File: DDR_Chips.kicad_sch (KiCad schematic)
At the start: 14 parts

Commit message: fix warnings
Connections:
- net DDR_BG0 renamed DDR4_BG0
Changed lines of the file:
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@@
     (effects (font (size 1.27 1.27)) (justify right))
   )
-  (hierarchical_label "DDR_BG0" (shape input) (at 30.48 96.52 180) (fields_autoplaced)
+  (hierarchical_label "DDR4_BG0" (shape input) (at 30.48 96.52 180) (fields_autoplaced)
     (effects (font (size 1.27 1.27)) (justify right))
   )

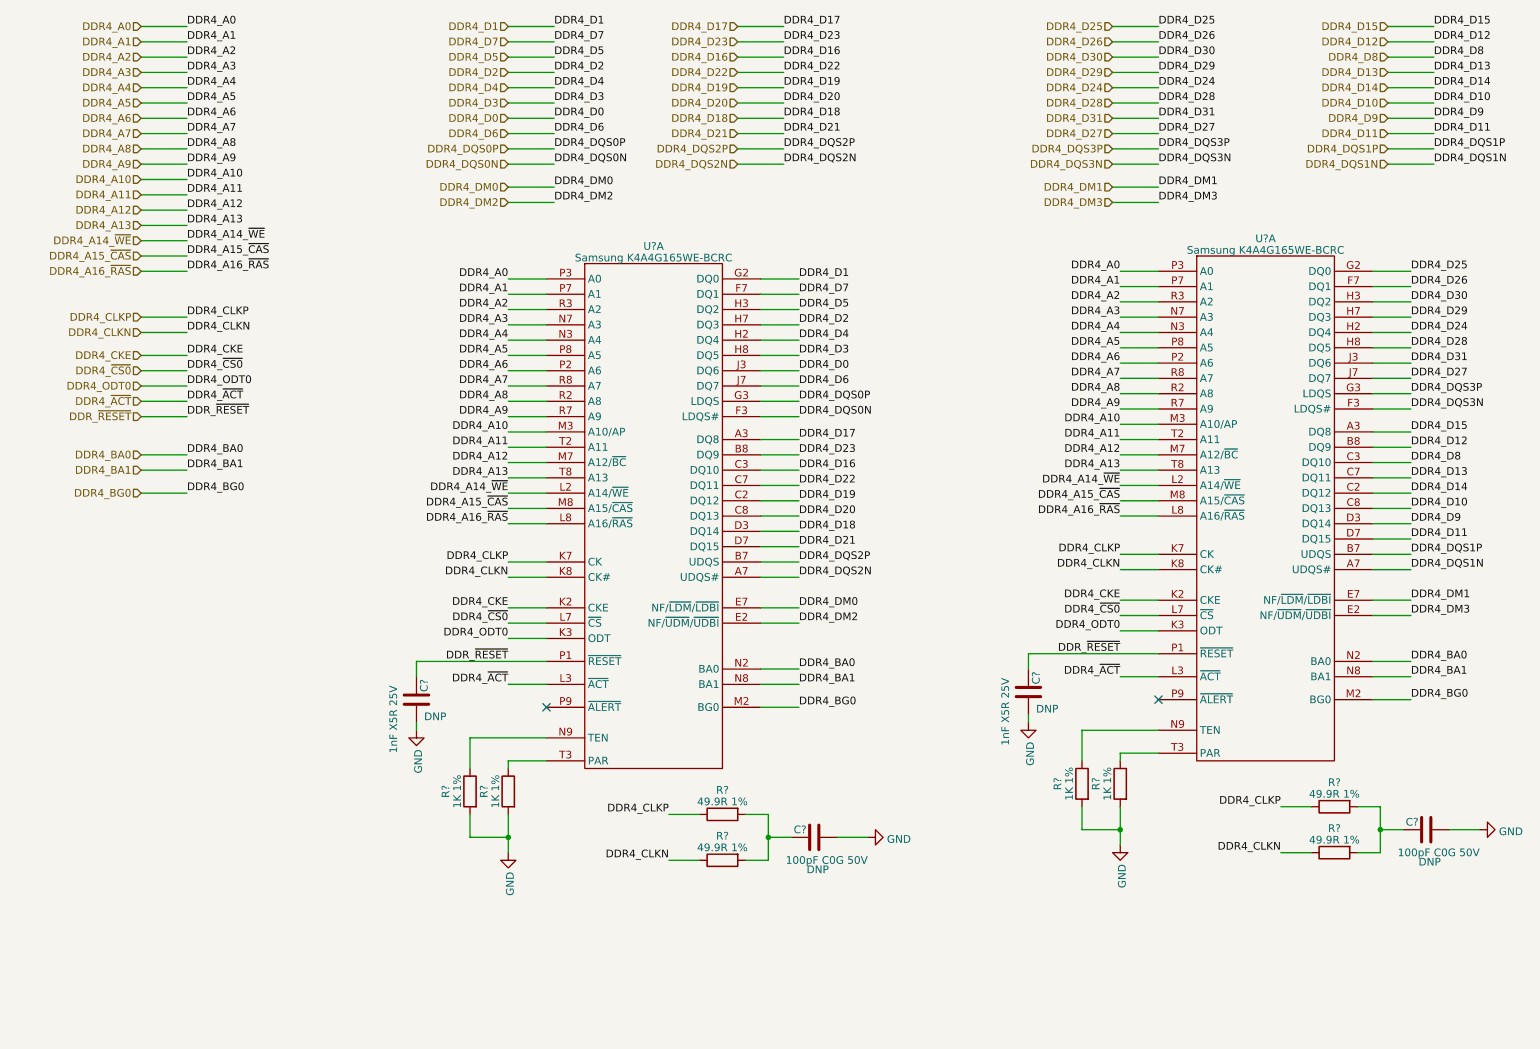
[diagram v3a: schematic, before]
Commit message: replace DDR4 chips with Hierachical Sheets module
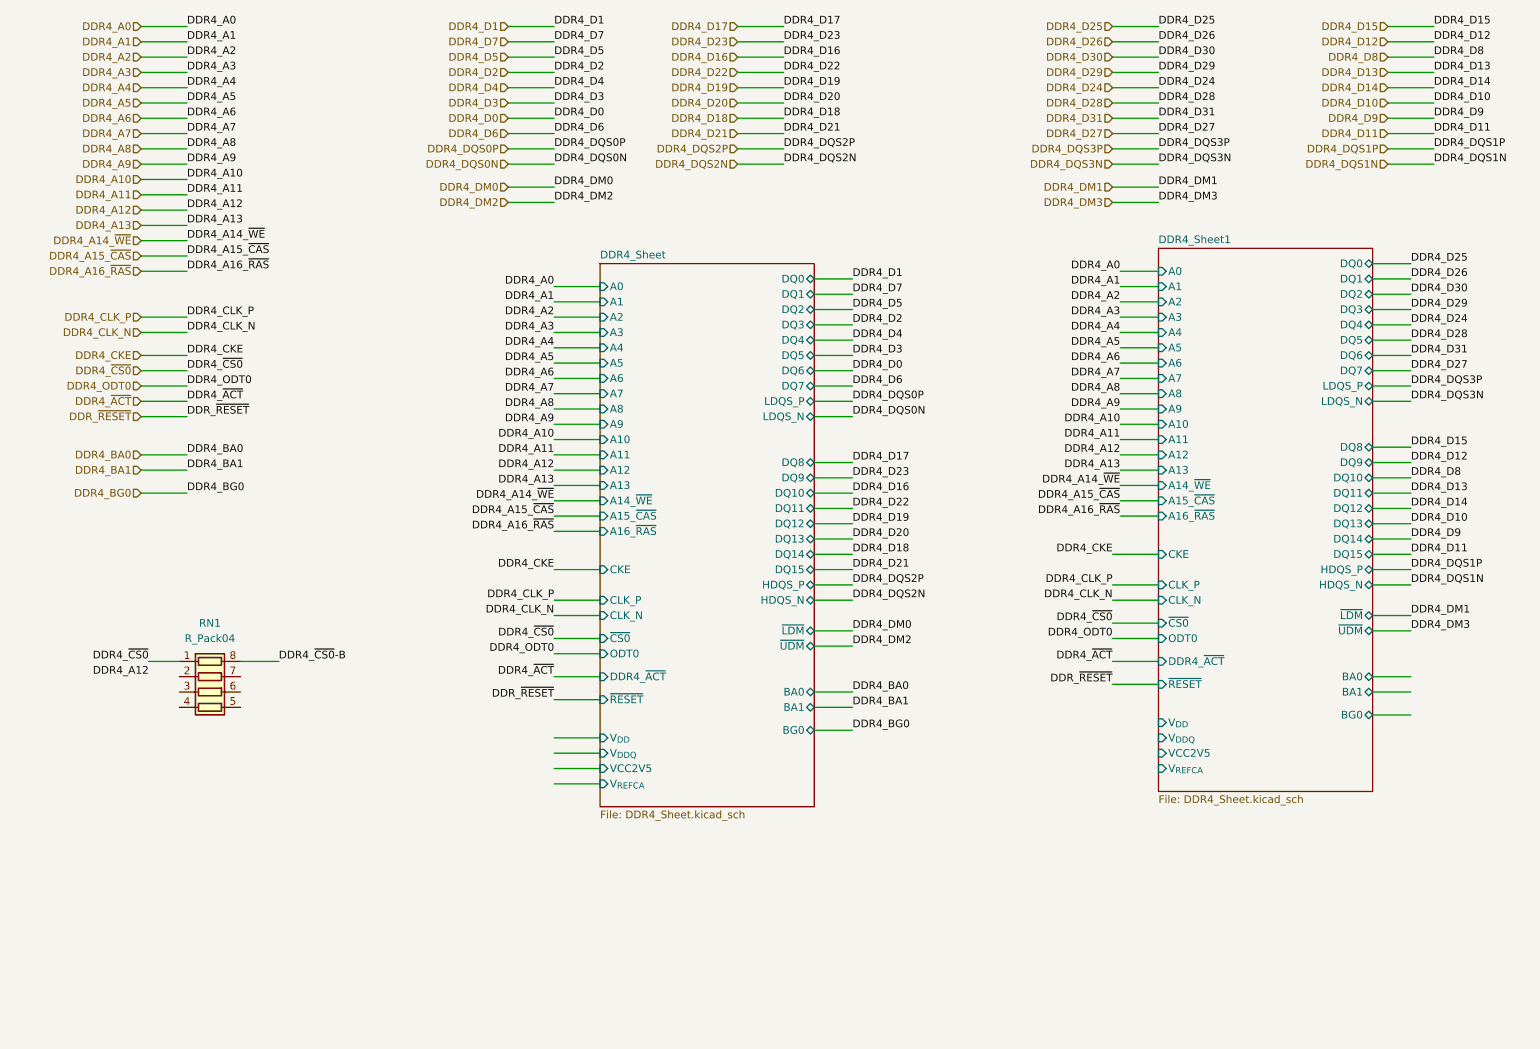
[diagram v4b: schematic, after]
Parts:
- removed C? (x2): 1nF X5R 25V, Capacitor_SMD:C_0201_0603Metric, symbol Device:C
- removed C? (x2): 100pF C0G 50V, Capacitor_SMD:C_0201_0603Metric, symbol Device:C
- removed R? (x4): 1K 1%, Resistor_SMD:R_0402_1005Metric, symbol Device:R
- removed R? (x4): 49.9R 1%, Resistor_SMD:R_0402_1005Metric, symbol Device:R
- removed U? (x2): Samsung K4A4G165WE-BCRC, Package_BGA:Micron_FBGA-96_9x14mm_Layout9x16_P0.8mm, symbol Memory_DDR:Micron_DDR4_MT40A512M16TB
- added RN1: R_Pack04, symbol Device:R_Pack04
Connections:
- net DDR4_~{CS0}: now also RN1.1 (R1.1)
- new net DDR4_~{CS0}-B: RN1.8 (R1.2)
- no-connect marks 2 -> 0
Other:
- added sheet DDR4_Sheet (DDR4_Sheet.kicad_sch)
- added sheet DDR4_Sheet1 (DDR4_Sheet.kicad_sch)
- note removed: "DNP"

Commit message: move DDR capacitors into DDR4_sheet
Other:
- added sheet DDR Filter Capacitors (DDR_filter_capacitors.kicad_sch)
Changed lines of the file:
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@@
+    (stroke (width 0) (type default))
+  )
+  (wire (pts (xy 35.56 172.72) (xy 43.18 172.72))
     (stroke (width 0) (type default))
   )
@@
   (label "DDR4_D22" (at 148.59 99.06 0) (fields_autoplaced)
     (effects (font (size 1.27 1.27)) (justify left bottom))
+  )
+  (label "VCC25_DDR" (at 35.56 172.72 180) (fields_autoplaced)
+    (effects (font (size 1.27 1.27)) (justify right bottom))
   )
   (label "DDR4_D10" (at 245.11 31.75 0) (fields_autoplaced)
@@
       )
     )
+  )
+  (sheet (at 43.18 157.48) (size 45.72 26.67) (fields_autoplaced)
+    (stroke (width 0.1524) (type solid))
+    (fill (color 0 0 0 0.0000))
+    (property "Sheetname" "DDR Filter Capacitors" (at 43.18 156.7684 0)
+      (effects (font (size 1.27 1.27)) (justify left bottom))
+    )
+    (property "Sheetfile" "DDR_filter_capacitors.kicad_sch" (at 43.18 184.7346 0)
+      (effects (font (size 1.27 1.27)) (justify left top))
+    )
+    (pin "VCC25_DDR" input (at 43.18 172.72 180)
+      (effects (font (size 1.27 1.27)) (justify left))
+    )
+    (instances
+      (project "leaf"
+        (path "/e3b58043-16a3-43c8-9fad-9c9784eebfa4/9453ad46-b3ff-4d4e-8aa6-7cc75aa0f522/43b336b1-9a2a-4a37-8b6d-a408b4dd9ca2" (page "19"))
+      )
+    )

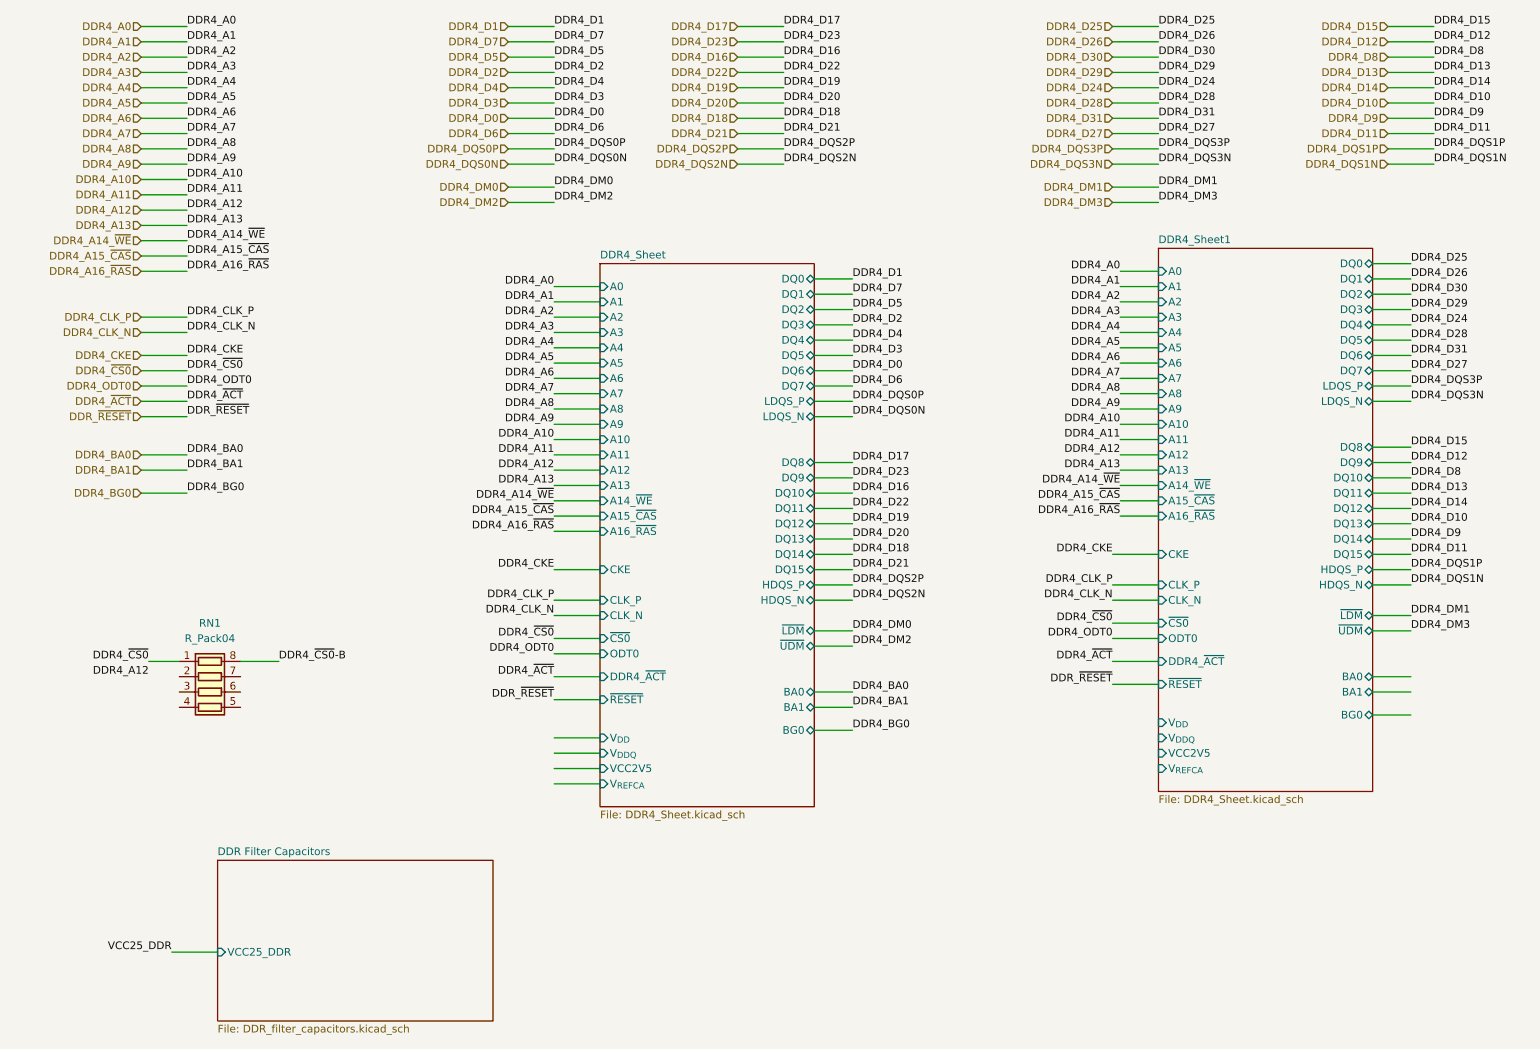
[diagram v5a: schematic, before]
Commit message: move DDR power decoupling capacitors into DDR4 Sheet
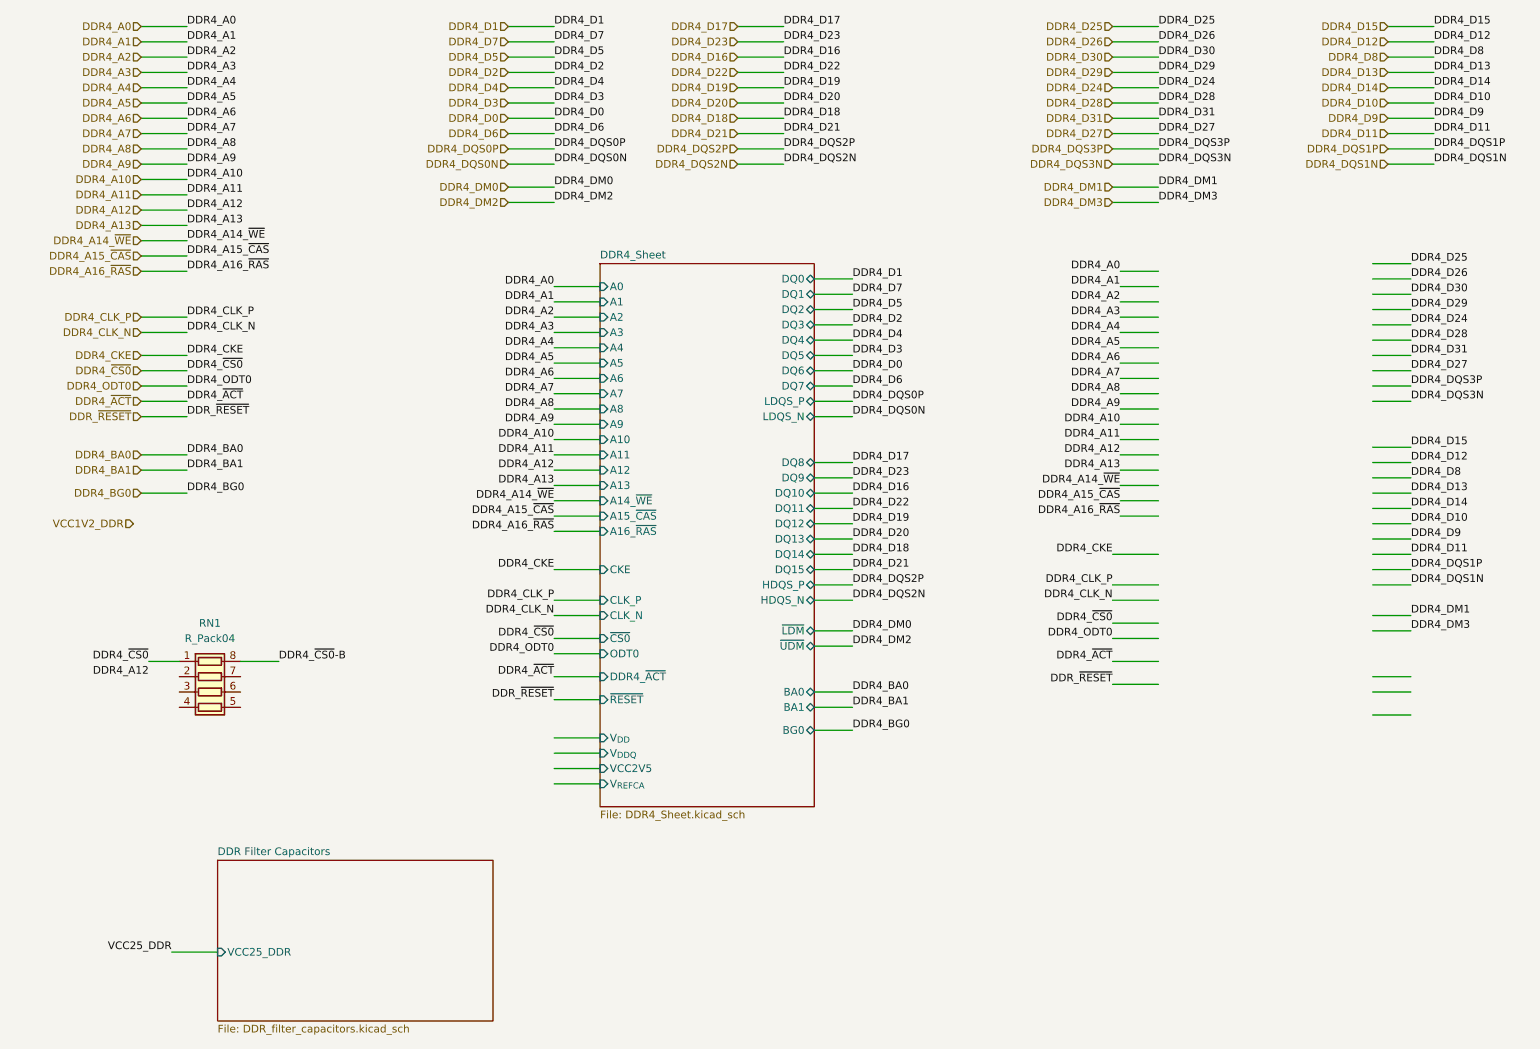
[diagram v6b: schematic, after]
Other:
- removed sheet DDR4_Sheet1
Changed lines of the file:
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@@
+    (effects (font (size 1.27 1.27)) (justify right))
+  )
+  (hierarchical_label "VCC1V2_DDR" (shape input) (at 29.21 101.6 180) (fields_autoplaced)
     (effects (font (size 1.27 1.27)) (justify right))
   )
@@
       )
     )
-  )
-  (sheet (at 199.39 55.88) (size 35.56 90.17) (fields_autoplaced)
-    (stroke (width 0.1524) (type solid))
-    (fill (color 0 0 0 0.0000))
-    (property "Sheetname" "DDR4_Sheet1" (at 199.39 55.1684 0)
-      (effects (font (size 1.27 1.27)) (justify left bottom))
-    )
-    (property "Sheetfile" "DDR4_Sheet.kicad_sch" (at 199.39 146.6346 0)
-      (effects (font (size 1.27 1.27)) (justify left top))
-    )
-    (pin "LDQS_P" bidirectional (at 234.95 78.74 0)
-      (effects (font (size 1.27 1.27)) (justify right))
-    )
-    (pin "DQ8" bidirectional (at 234.95 88.9 0)
-      (effects (font (size 1.27 1.27)) (justify right))
-    )
-    (pin "DQ6" bidirectional (at 234.95 73.66 0)
-      (effects (font (size 1.27 1.27)) (justify right))
-    )
-    (pin "DQ9" bidirectional (at 234.95 91.44 0)
-      (effects (font (size 1.27 1.27)) (justify right))
-    )
-    (pin "DQ7" bidirectional (at 234.95 76.2 0)
-      (effects (font (size 1.27 1.27)) (justify right))
-    )
-    (pin "DQ1" bidirectional (at 234.95 60.96 0)
-      (effects (font (size 1.27 1.27)) (justify right))
-    )
-    (pin "DQ4" bidirectional (at 234.95 68.58 0)
-      (effects (font (size 1.27 1.27)) (justify right))
-    )
-    (pin "DQ0" bidirectional (at 234.95 58.42 0)
-      (effects (font (size 1.27 1.27)) (justify right))
-    )
-    (pin "DQ2" bidirectional (at 234.95 63.5 0)
-      (effects (font (size 1.27 1.27)) (justify right))
-    )
-    (pin "DQ5" bidirectional (at 234.95 71.12 0)
-      (effects (font (size 1.27 1.27)) (justify right))
-    )
-    (pin "DQ3" bidirectional (at 234.95 66.04 0)
-      (effects (font (size 1.27 1.27)) (justify right))
-    )
-    (pin "DQ13" bidirectional (at 234.95 101.6 0)
-      (effects (font (size 1.27 1.27)) (justify right))
-    )
-    (pin "DQ14" bidirectional (at 234.95 104.14 0)
-      (effects (font (size 1.27 1.27)) (justify right))
-    )
-    (pin "DQ11" bidirectional (at 234.95 96.52 0)
-      (effects (font (size 1.27 1.27)) (justify right))
-    )
-    (pin "DQ15" bidirectional (at 234.95 106.68 0)
-      (effects (font (size 1.27 1.27)) (justify right))
-    )
-    (pin "DQ12" bidirectional (at 234.95 99.06 0)
-      (effects (font (size 1.27 1.27)) (justify right))
-    )
-    (pin "HDQS_P" bidirectional (at 234.95 109.22 0)
-      (effects (font (size 1.27 1.27)) (justify right))
-    )
-    (pin "~{UDM}" bidirectional (at 234.95 119.38 0)
-      (effects (font (size 1.27 1.27)) (justify right))
-    )
-    (pin "~{LDM}" bidirectional (at 234.95 116.84 0)
-      (effects (font (size 1.27 1.27)) (justify right))
-    )
-    (pin "BA0" bidirectional (at 234.95 127 0)
-      (effects (font (size 1.27 1.27)) (justify right))
-    )
-    (pin "BA1" bidirectional (at 234.95 129.54 0)
-      (effects (font (size 1.27 1.27)) (justify right))
-    )
-    (pin "BG0" bidirectional (at 234.95 133.35 0)
-      (effects (font (size 1.27 1.27)) (justify right))
-    )
-    (pin "LDQS_N" bidirectional (at 234.95 81.28 0)
-      (effects (font (size 1.27 1.27)) (justify right))
-    )
-    (pin "DQ10" bidirectional (at 234.95 93.98 0)
-      (effects (font (size 1.27 1.27)) (justify right))
-    )
-    (pin "HDQS_N" bidirectional (at 234.95 111.76 0)
-      (effects (font (size 1.27 1.27)) (justify right))
-    )
-    (pin "DDR4_~{ACT}" input (at 199.39 124.46 180)
-      (effects (font (size 1.27 1.27)) (justify left))
-    )
-    (pin "~{RESET}" input (at 199.39 128.27 180)
-      (effects (font (size 1.27 1.27)) (justify left))
-    )
-    (pin "CLK_N" input (at 199.39 114.3 180)
-      (effects (font (size 1.27 1.27)) (justify left))
-    )
-    (pin "CKE" input (at 199.39 106.68 180)
-      (effects (font (size 1.27 1.27)) (justify left))
-    )
-    (pin "~{CS0}" input (at 199.39 118.11 180)
-      (effects (font (size 1.27 1.27)) (justify left))
-    )
-    (pin "ODT0" input (at 199.39 120.65 180)
-      (effects (font (size 1.27 1.27)) (justify left))
-    )
-    (pin "A6" input (at 199.39 74.93 180)
-      (effects (font (size 1.27 1.27)) (justify left))
-    )
-    (pin "A7" input (at 199.39 77.47 180)
-      (effects (font (size 1.27 1.27)) (justify left))
-    )
-    (pin "A15_~{CAS}" input (at 199.39 97.79 180)
-      (effects (font (size 1.27 1.27)) (justify left))
-    )
-    (pin "A16_~{RAS}" input (at 199.39 100.33 180)
-      (effects (font (size 1.27 1.27)) (justify left))
-    )
-    (pin "A14_~{WE}" input (at 199.39 95.25 180)
-      (effects (font (size 1.27 1.27)) (justify left))
-    )
-    (pin "CLK_P" input (at 199.39 111.76 180)
-      (effects (font (size 1.27 1.27)) (justify left))
-    )
-    (pin "A5" input (at 199.39 72.39 180)
-      (effects (font (size 1.27 1.27)) (justify left))
-    )
-    (pin "A2" input (at 199.39 64.77 180)
-      (effects (font (size 1.27 1.27)) (justify left))
-    )
-    (pin "A0" input (at 199.39 59.69 180)
-      (effects (font (size 1.27 1.27)) (justify left))
-    )
-    (pin "A3" input (at 199.39 67.31 180)
-      (effects (font (size 1.27 1.27)) (justify left))
-    )
-    (pin "A1" input (at 199.39 62.23 180)
-      (effects (font (size 1.27 1.27)) (justify left))
-    )
-    (pin "A4" input (at 199.39 69.85 180)
-      (effects (font (size 1.27 1.27)) (justify left))
-    )
-    (pin "A8" input (at 199.39 80.01 180)
-      (effects (font (size 1.27 1.27)) (justify left))
-    )
-    (pin "A9" input (at 199.39 82.55 180)
-      (effects (font (size 1.27 1.27)) (justify left))
-    )
-    (pin "A10" input (at 199.39 85.09 180)
-      (effects (font (size 1.27 1.27)) (justify left))
-    )
-    (pin "A11" input (at 199.39 87.63 180)
-      (effects (font (size 1.27 1.27)) (justify left))
-    )
-    (pin "A12" input (at 199.39 90.17 180)
-      (effects (font (size 1.27 1.27)) (justify left))
-    )
-    (pin "A13" input (at 199.39 92.71 180)
-      (effects (font (size 1.27 1.27)) (justify left))
-    )
-    (pin "V_{DD}" input (at 199.39 134.62 180)
-      (effects (font (size 1.27 1.27)) (justify left))
-    )
-    (pin "VCC2V5" input (at 199.39 139.7 180)
-      (effects (font (size 1.27 1.27)) (justify left))
-    )
-    (pin "V_{DDQ}" input (at 199.39 137.16 180)
-      (effects (font (size 1.27 1.27)) (justify left))
-    )
-    (pin "V_{REFCA}" input (at 199.39 142.24 180)
-      (effects (font (size 1.27 1.27)) (justify left))
-    )
-    (instances
-      (project "leaf"
-        (path "/e3b58043-16a3-43c8-9fad-9c9784eebfa4/9453ad46-b3ff-4d4e-8aa6-7cc75aa0f522/43b336b1-9a2a-4a37-8b6d-a408b4dd9ca2" (page "17"))
-      )
-    )

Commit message: changed Power Label and copy DDR4 Sheets
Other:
- added sheet DDR4_Sheet1 (DDR4_Sheet.kicad_sch)
- sheet DDR4_Sheet ports: added VCC1V2; removed V_{DDQ}, V_{DD}
